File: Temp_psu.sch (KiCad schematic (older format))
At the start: 2 parts

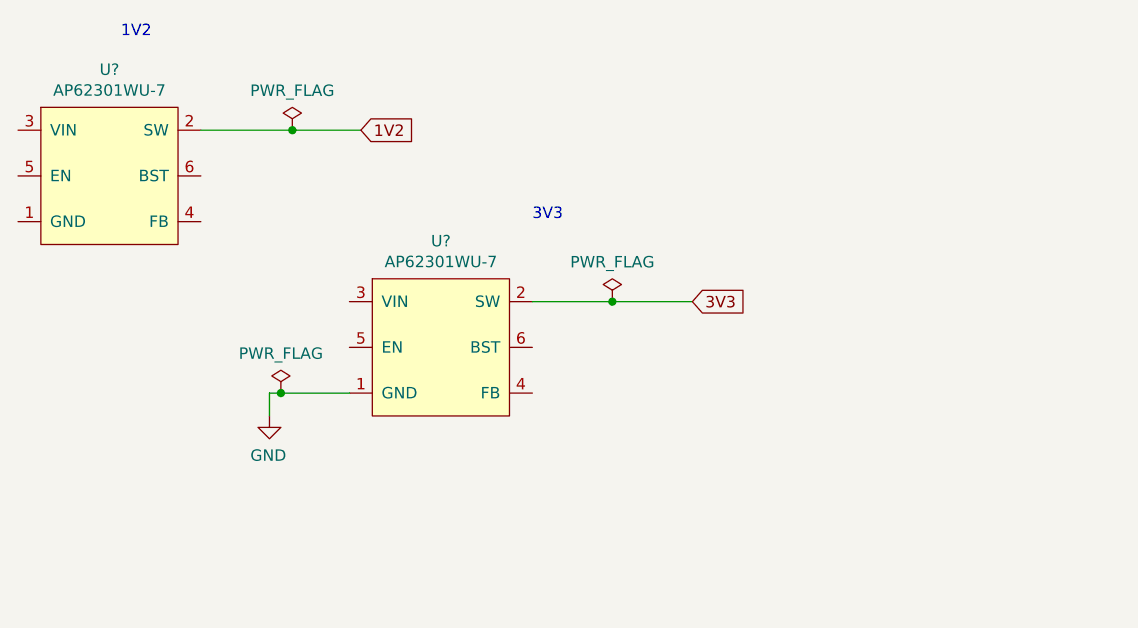
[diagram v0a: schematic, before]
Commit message: add 1V8 converter
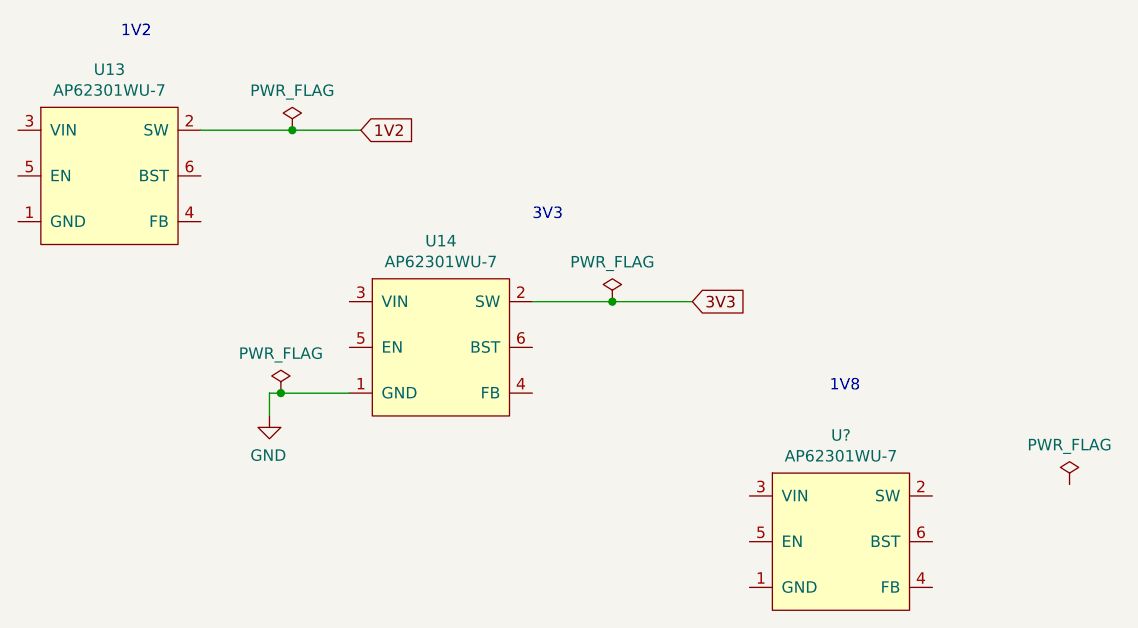
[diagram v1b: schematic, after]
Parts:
- added U?: AP62301WU-7, antmicro-footprints:TSOT23-6, symbol antmicroDCDCConverters:AP62301WU-7
- gave numbers to parts that had none: 2
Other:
- note added: "1V8\n"
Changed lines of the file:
@@
 P 1650 1550
 AR Path="/61B0DC30/61DC322E" Ref="U?"  Part="1"
-AR Path="/61DC2BE0/61DC322E" Ref="U?"  Part="1"
-F 0 "U?" H 1650 2015 50  0000 C CNN
+AR Path="/61DC2BE0/61DC322E" Ref="U13"  Part="1"
+F 0 "U13" H 1650 2015 50  0000 C CNN
 F 1 "AP62301WU-7" H 1650 1924 50  0000 C CNN
 F 2 "sa800u-baseboard-hw-footprints:TSOT23-6" H 1600 900 50  0001 C CNN
@@
 P 3100 2300
 AR Path="/61B0DC30/61DC3236" Ref="U?"  Part="1"
-AR Path="/61DC2BE0/61DC3236" Ref="U?"  Part="1"
-F 0 "U?" H 3100 2765 50  0000 C CNN
+AR Path="/61DC2BE0/61DC3236" Ref="U14"  Part="1"
+F 0 "U14" H 3100 2765 50  0000 C CNN
 F 1 "AP62301WU-7" H 3100 2674 50  0000 C CNN
 F 2 "sa800u-baseboard-hw-footprints:TSOT23-6" H 3050 1650 50  0001 C CNN
@@
 P 2350 2600
 AR Path="/61B0DC30/61DC3242" Ref="#PWR?"  Part="1"
-AR Path="/61DC2BE0/61DC3242" Ref="#PWR?"  Part="1"
-F 0 "#PWR?" H 2350 2350 50  0001 C CNN
+AR Path="/61DC2BE0/61DC3242" Ref="#PWR0164"  Part="1"
+F 0 "#PWR0164" H 2350 2350 50  0001 C CNN
 F 1 "GND" H 2355 2427 50  0000 C CNN
 F 2 "" H 2350 2600 50  0001 C CNN
@@
 P 3850 2100
 AR Path="/61B0DC30/61DC3248" Ref="#FLG?"  Part="1"
-AR Path="/61DC2BE0/61DC3248" Ref="#FLG?"  Part="1"
-F 0 "#FLG?" H 3850 2175 50  0001 C CNN
+AR Path="/61DC2BE0/61DC3248" Ref="#FLG0101"  Part="1"
+F 0 "#FLG0101" H 3850 2175 50  0001 C CNN
 F 1 "PWR_FLAG" H 3850 2273 50  0000 C CNN
 F 2 "" H 3850 2100 50  0001 C CNN
@@
 P 2400 2500
 AR Path="/61B0DC30/61DC3250" Ref="#FLG?"  Part="1"
-AR Path="/61DC2BE0/61DC3250" Ref="#FLG?"  Part="1"
-F 0 "#FLG?" H 2400 2575 50  0001 C CNN
+AR Path="/61DC2BE0/61DC3250" Ref="#FLG0102"  Part="1"
+F 0 "#FLG0102" H 2400 2575 50  0001 C CNN
 F 1 "PWR_FLAG" H 2400 2673 50  0000 C CNN
 F 2 "" H 2400 2500 50  0001 C CNN
@@
 P 2450 1350
 AR Path="/61B0DC30/61DC3258" Ref="#FLG?"  Part="1"
-AR Path="/61DC2BE0/61DC3258" Ref="#FLG?"  Part="1"
-F 0 "#FLG?" H 2450 1425 50  0001 C CNN
+AR Path="/61DC2BE0/61DC3258" Ref="#FLG0103"  Part="1"
+F 0 "#FLG0103" H 2450 1425 50  0001 C CNN
 F 1 "PWR_FLAG" H 2450 1523 50  0000 C CNN
 F 2 "" H 2450 1350 50  0001 C CNN
@@
 Wire Wire Line
 	2450 1350 2750 1350
+$Comp
+L antmicroDCDCConverters:AP62301WU-7 U?
+U 1 1 61F9EBD9
+P 4850 3150
+F 0 "U?" H 4850 3615 50  0000 C CNN
+F 1 "AP62301WU-7" H 4850 3524 50  0000 C CNN
+F 2 "antmicro-footprints:TSOT23-6" H 4800 2500 50  0001 C CNN
+F 3 "https://www.diodes.com/assets/Datasheets/AP62300_AP62301_AP62300T.pdf" H 4800 2800 50  0001 C CNN
+F 4 "AP62301WU-7" H 4800 2600 50  0001 C CNN "MPN"
+F 5 "Diodes Incorporated" H 4800 2700 50  0001 C CNN "Manufacturer"
+	1    4850 3150
+	1    0    0    -1
+$EndComp
+Text Notes 4800 2500 0    50   ~ 0
+1V8\n
+$Comp
+L power:PWR_FLAG #FLG?
+U 1 1 61F9EE21
+P 5850 2900
+AR Path="/61B0DC30/61F9EE21" Ref="#FLG?"  Part="1"
+AR Path="/61DC2BE0/61F9EE21" Ref="#FLG?"  Part="1"
+F 0 "#FLG?" H 5850 2975 50  0001 C CNN
+F 1 "PWR_FLAG" H 5850 3073 50  0000 C CNN
+F 2 "" H 5850 2900 50  0001 C CNN
+F 3 "~" H 5850 2900 50  0001 C CNN
+	1    5850 2900
+	1    0    0    -1
+$EndComp
 $EndSCHEMATC

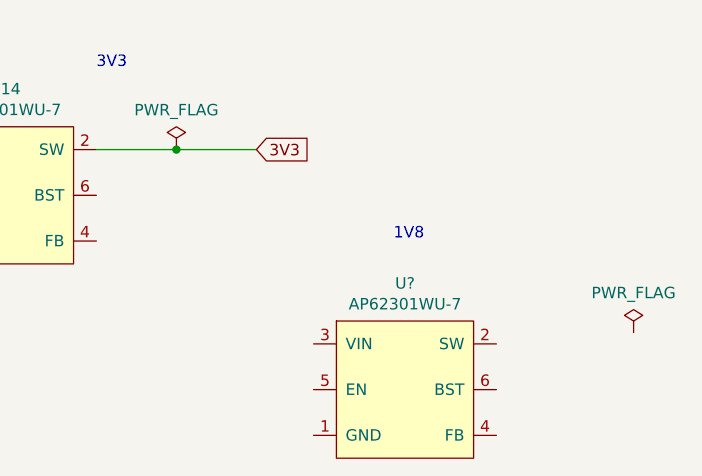
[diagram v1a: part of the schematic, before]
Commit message: fixing ERC errors
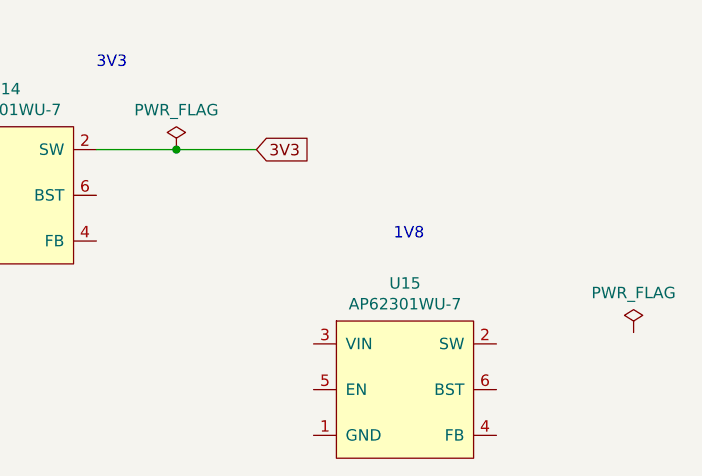
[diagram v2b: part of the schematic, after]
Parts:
- gave numbers to parts that had none: 1
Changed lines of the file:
@@
 U 1 1 61F9EBD9
 P 4850 3150
-F 0 "U?" H 4850 3615 50  0000 C CNN
+AR Path="/61B0DC30/61F9EBD9" Ref="U?"  Part="1"
+AR Path="/61DC2BE0/61F9EBD9" Ref="U15"  Part="1"
+F 0 "U15" H 4850 3615 50  0000 C CNN
 F 1 "AP62301WU-7" H 4850 3524 50  0000 C CNN
 F 2 "antmicro-footprints:TSOT23-6" H 4800 2500 50  0001 C CNN
@@
 P 5850 2900
 AR Path="/61B0DC30/61F9EE21" Ref="#FLG?"  Part="1"
-AR Path="/61DC2BE0/61F9EE21" Ref="#FLG?"  Part="1"
-F 0 "#FLG?" H 5850 2975 50  0001 C CNN
+AR Path="/61DC2BE0/61F9EE21" Ref="#FLG0107"  Part="1"
+F 0 "#FLG0107" H 5850 2975 50  0001 C CNN
 F 1 "PWR_FLAG" H 5850 3073 50  0000 C CNN
 F 2 "" H 5850 2900 50  0001 C CNN

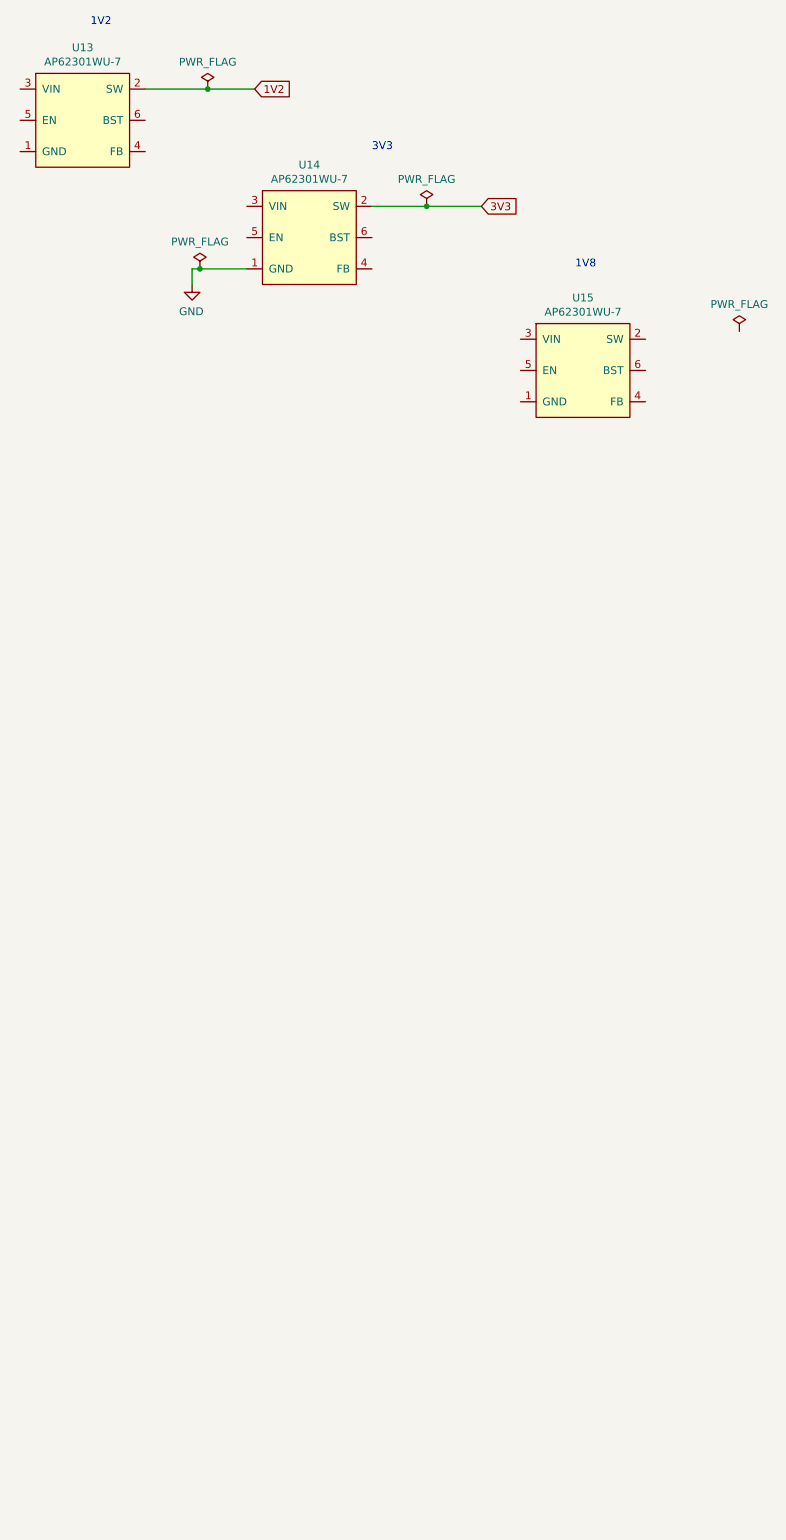
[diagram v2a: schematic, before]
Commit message: Populate DCDCs with passives
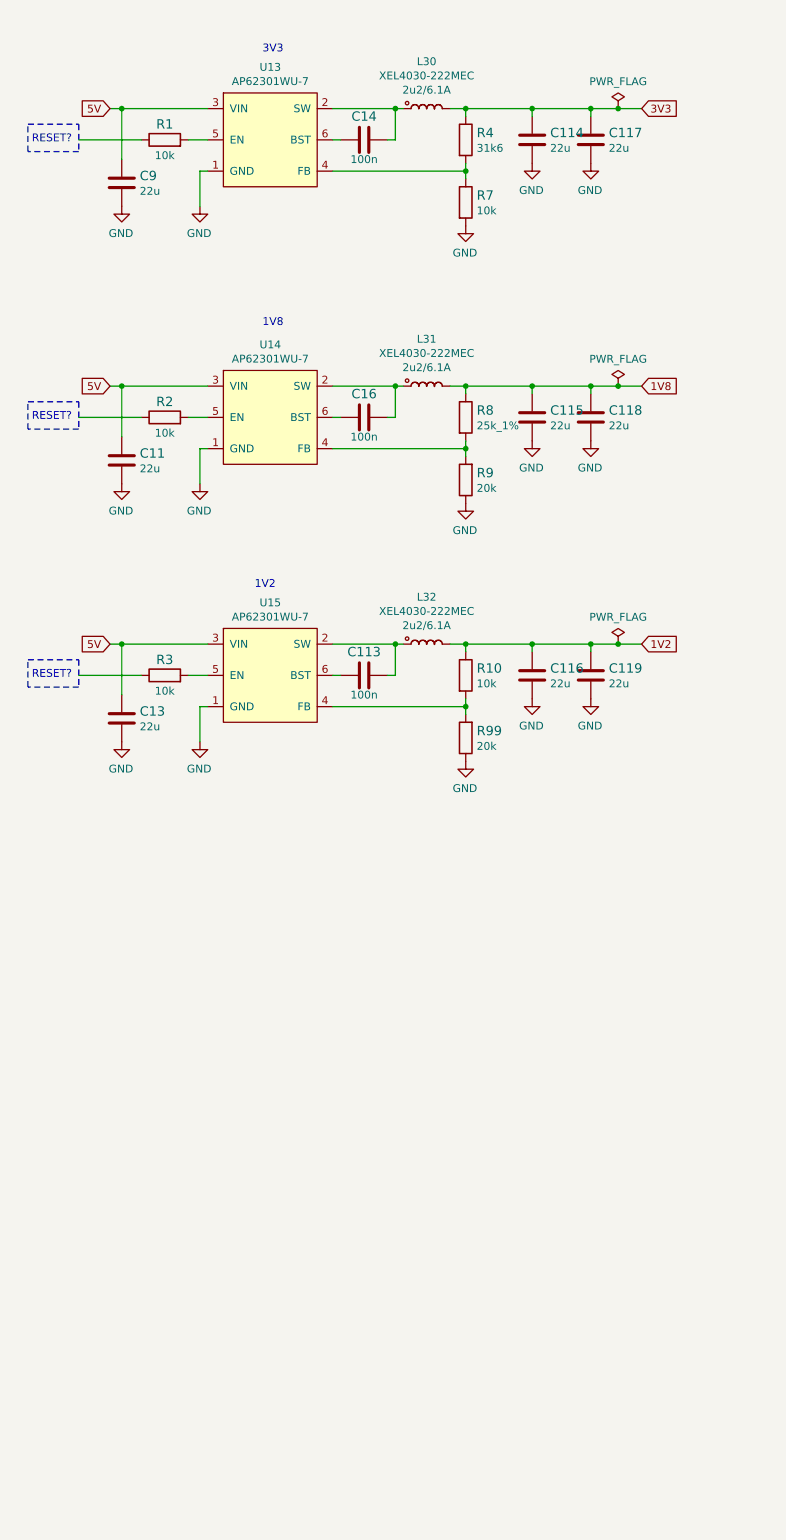
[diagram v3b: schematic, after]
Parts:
- removed U15: AP62301WU-7, antmicro-footprints:TSOT23-6, symbol antmicroDCDCConverters:AP62301WU-7
- added C11, C114, C115, C116, C117, C118, C119, C13, C9: C_22u_0603, antmicro-footprints:0603-cap, symbol antmicroCapacitors0603:C_22u_0603
- added C113, C14, C16: C_100n_0402, sa800u-baseboard-hw-footprints:0402-cap, symbol sa800u-baseboard-hw:C_100n_0402
- added L30, L31, L32: XEL4030-222MEC, antmicro-footprints:Coilcraft-XEL4030, symbol antmicroFixedInductors:XEL4030-222MEC
- added R1, R10, R2, R3, R7: R_10k_0402, antmicro-footprints:0402-res, symbol antmicroResistors0402:R_10k_0402
- added R4: R_31k6_0402, antmicro-footprints:0402-res, symbol antmicroResistors0402:R_31k6_0402
- added R8: R_25k_1%_0402, antmicro-footprints:0402, symbol antmicroResistors0402:R_25k_1%_0402
- added R9, R99: R_20k_0402, antmicro-footprints:0402-res, symbol antmicroResistors0402:R_20k_0402
- added U15: AP62301WU-7, sa800u-baseboard-hw-footprints:TSOT23-6, symbol sa800u-baseboard-hw:AP62301WU-7
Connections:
- net labels added: 1V8, 5V
- wire segments 7 -> 69
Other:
- note added: "RESET?"
- moved on the sheet: U13

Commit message: Add USB debug circuitry, loclib
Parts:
- removed C11, C114, C115, C116, C117, C118, C119, C13, C9: C_22u_0603, antmicro-footprints:0603-cap, symbol antmicroCapacitors0603:C_22u_0603
- removed L30, L31: XEL4030-222MEC, antmicro-footprints:Coilcraft-XEL4030, symbol antmicroFixedInductors:XEL4030-222MEC
- removed R1, R10, R2, R3, R7: R_10k_0402, antmicro-footprints:0402-res, symbol antmicroResistors0402:R_10k_0402
- removed R4: R_31k6_0402, antmicro-footprints:0402-res, symbol antmicroResistors0402:R_31k6_0402
- added C11, C114, C115, C116, C117, C118, C119, C13, C9: C_22u_0603, sa800u-baseboard-hw-footprints:0603-cap, symbol sa800u-baseboard-hw:C_22u_0603
- added L30, L31: XEL4030-222MEC, sa800u-baseboard-hw-footprints:Coilcraft-XEL4030, symbol sa800u-baseboard-hw:XEL4030-222MEC
- added R1, R10, R2, R3, R7: R_10k_0402, sa800u-baseboard-hw-footprints:0402-res, symbol sa800u-baseboard-hw:R_10k_0402
- added R4: R_31k6_0402, sa800u-baseboard-hw-footprints:0402-res, symbol sa800u-baseboard-hw:R_31k6_0402
- L32: footprint antmicro-footprints:Coilcraft-XEL4030 -> sa800u-baseboard-hw-footprints:Coilcraft-XEL4030; symbol antmicroFixedInductors:XEL4030-222MEC -> sa800u-baseboard-hw:XEL4030-222MEC
- R8: footprint antmicro-footprints:0402 -> sa800u-baseboard-hw-footprints:0402; symbol antmicroResistors0402:R_25k_1%_0402 -> sa800u-baseboard-hw:R_25k_1%_0402
- R9, R99: footprint antmicro-footprints:0402-res -> sa800u-baseboard-hw-footprints:0402-res; symbol antmicroResistors0402:R_20k_0402 -> sa800u-baseboard-hw:R_20k_0402
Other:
- moved on the sheet: L32, R8, R9, R99

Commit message: Move parts from tmp to PSU.sch
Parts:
- removed C11, C114, C115, C116, C117, C118, C119, C13, C9: C_22u_0603, sa800u-baseboard-hw-footprints:0603-cap, symbol sa800u-baseboard-hw:C_22u_0603
- removed C113, C14, C16: C_100n_0402, sa800u-baseboard-hw-footprints:0402-cap, symbol sa800u-baseboard-hw:C_100n_0402
- removed L30, L31, L32: XEL4030-222MEC, sa800u-baseboard-hw-footprints:Coilcraft-XEL4030, symbol sa800u-baseboard-hw:XEL4030-222MEC
- removed R1, R10, R2, R3, R7: R_10k_0402, sa800u-baseboard-hw-footprints:0402-res, symbol sa800u-baseboard-hw:R_10k_0402
- removed R4: R_31k6_0402, sa800u-baseboard-hw-footprints:0402-res, symbol sa800u-baseboard-hw:R_31k6_0402
- removed R8: R_25k_1%_0402, sa800u-baseboard-hw-footprints:0402, symbol sa800u-baseboard-hw:R_25k_1%_0402
- removed R9, R99: R_20k_0402, sa800u-baseboard-hw-footprints:0402-res, symbol sa800u-baseboard-hw:R_20k_0402
- removed U13, U14, U15: AP62301WU-7, sa800u-baseboard-hw-footprints:TSOT23-6, symbol sa800u-baseboard-hw:AP62301WU-7
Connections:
- net labels removed: 1V2, 1V8, 3V3, 5V, GND
- wire segments 69 -> 0
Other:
- note removed: "1V2\n"
- note removed: "1V8\n"
- note removed: "3V3"
- note removed: "RESET?"
